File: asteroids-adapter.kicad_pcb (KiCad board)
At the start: 2 copper layers, 88 x 90.2 mm, 15 parts, among them J1 Asteroids PCB connector, J2 Asteroids harness connector, U1 TL074

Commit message: Update to rev 1.3
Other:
- board text added: "Asteroids <-> Ast Deluxe Cabinet Adapter rev 1.3"
- board text removed: "Asteroids <-> Ast Deluxe Cabinet Adapter rev 1.2"
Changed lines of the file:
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@@
   (title_block
     (title "Asteroids to Asteroids Deluxe Adapter")
-    (date "2022-02-22")
-    (rev "1.2")
+    (date "2022-02-24")
+    (rev "1.3")
   )
   (layers
@@
     (effects (font (size 1.905 1.905) (thickness 0.3)) (justify mirror))
   )
-  (gr_text "Asteroids <-> Ast Deluxe Cabinet Adapter rev 1.2" (at 150.5204 62.5856) (layer "F.SilkS")
+  (gr_text "Asteroids <-> Ast Deluxe Cabinet Adapter rev 1.3" (at 150.5204 62.5856) (layer "F.SilkS")
     (effects (font (size 1.524 1.524) (thickness 0.3)))
   )

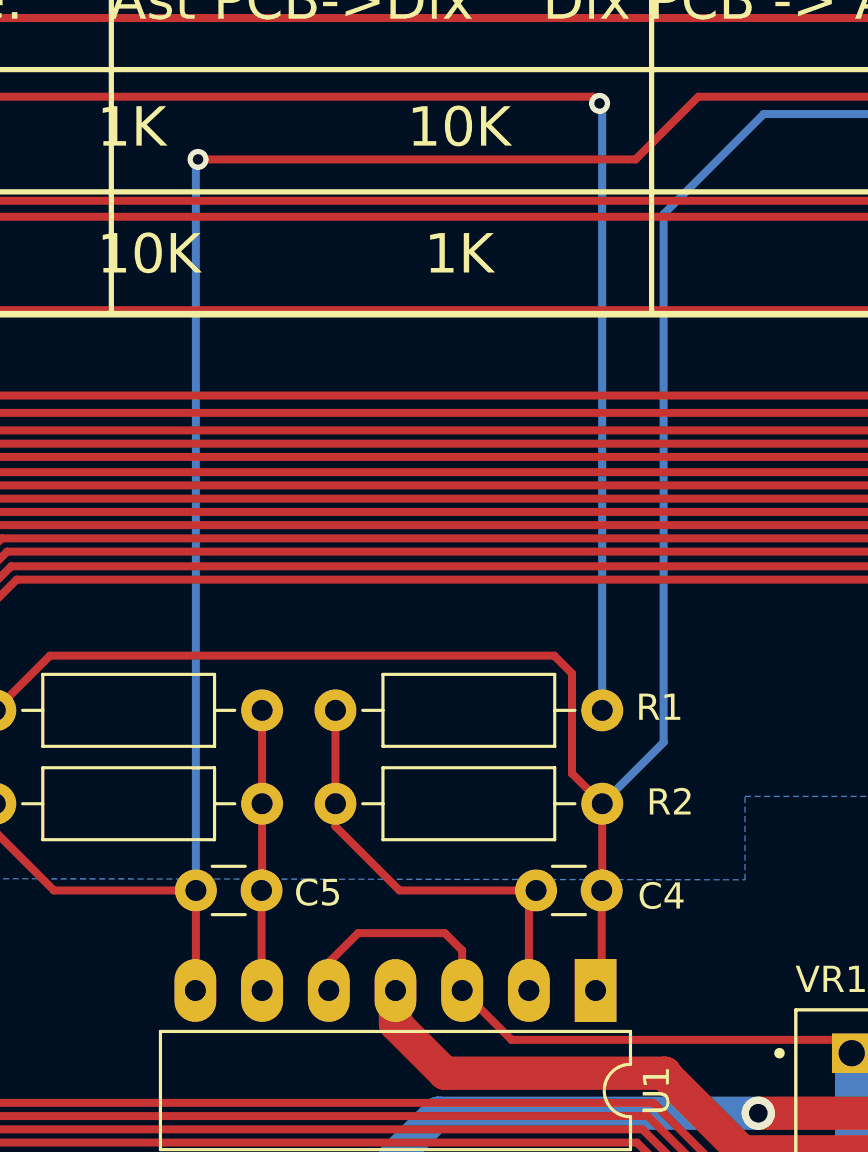
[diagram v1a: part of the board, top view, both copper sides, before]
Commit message: Add bypass to 5V op-amp reference
- Added 10 uf cap at (+) input of both audio inverter op amps, to reduce
noise.
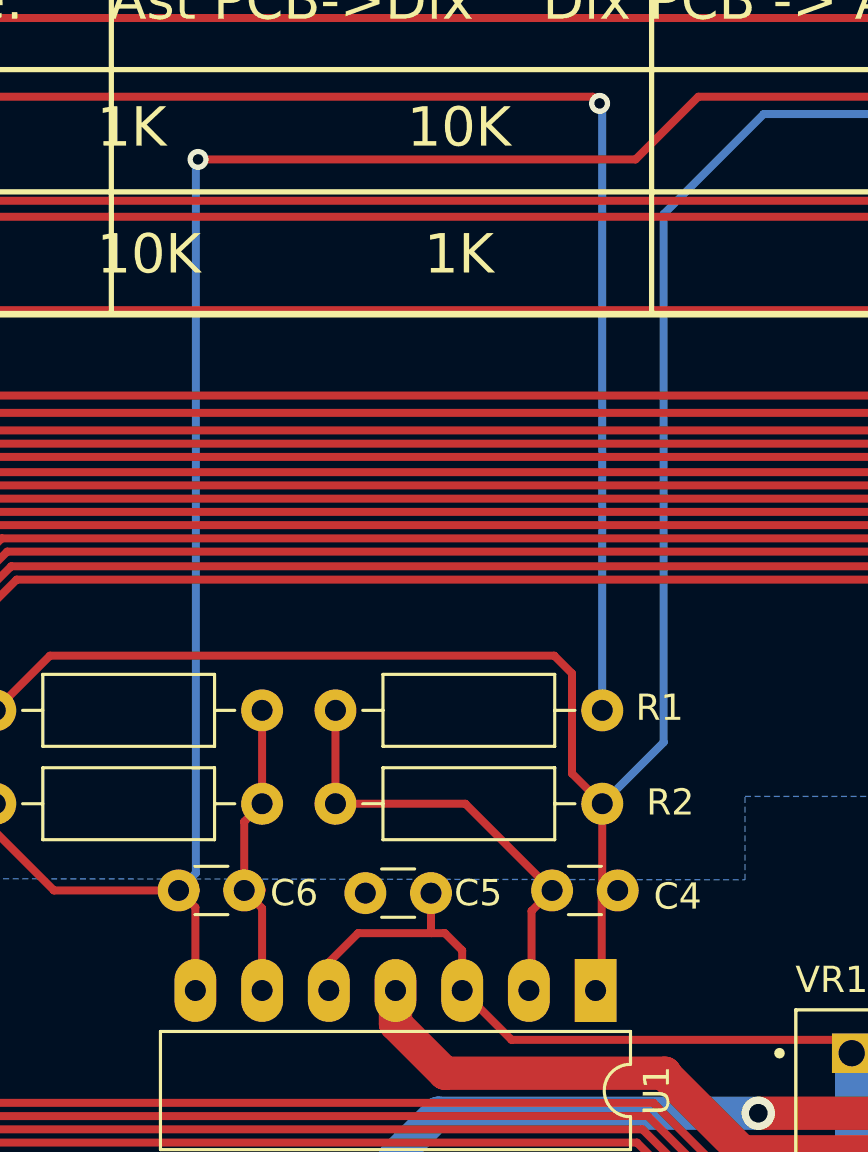
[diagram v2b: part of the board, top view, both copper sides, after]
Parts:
- added C5: Kemet 10 uF 25V MLCC TH, Capacitor_THT:C_Disc_D3.0mm_W1.6mm_P2.50mm, F.Cu at (143.0, 102.1)
- moved C6 0.66 mm to (138.4, 102.0)
- moved C4 0.61 mm to (150.1, 102.0)
- renumbered C5 to C6
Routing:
- net +5V: track 129.9 -> 131.4 mm
- net Net-(C6-Pad1): track 10.7 -> 11.3 mm
- net Audio_2_out: track 96.4 -> 96.9 mm

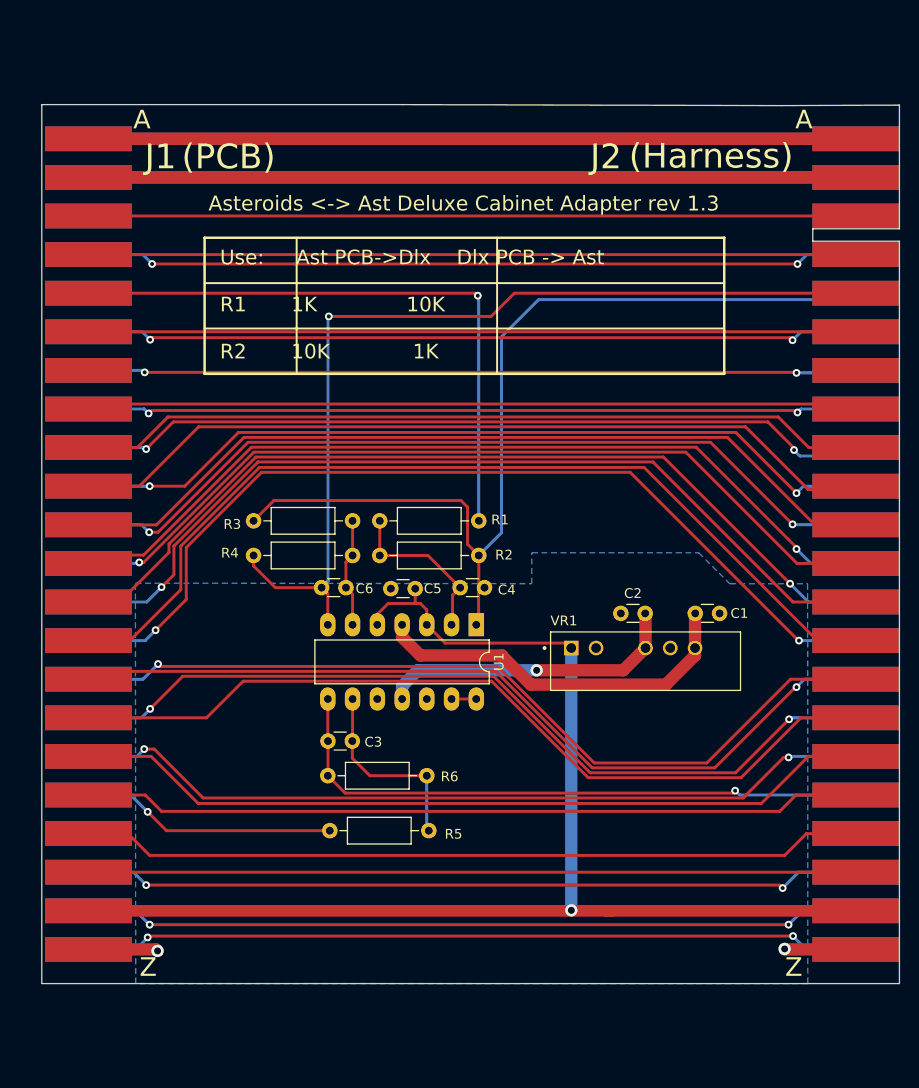
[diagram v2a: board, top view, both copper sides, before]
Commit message: Move parts for narrower design
- Still need to move connector and finish re-routing
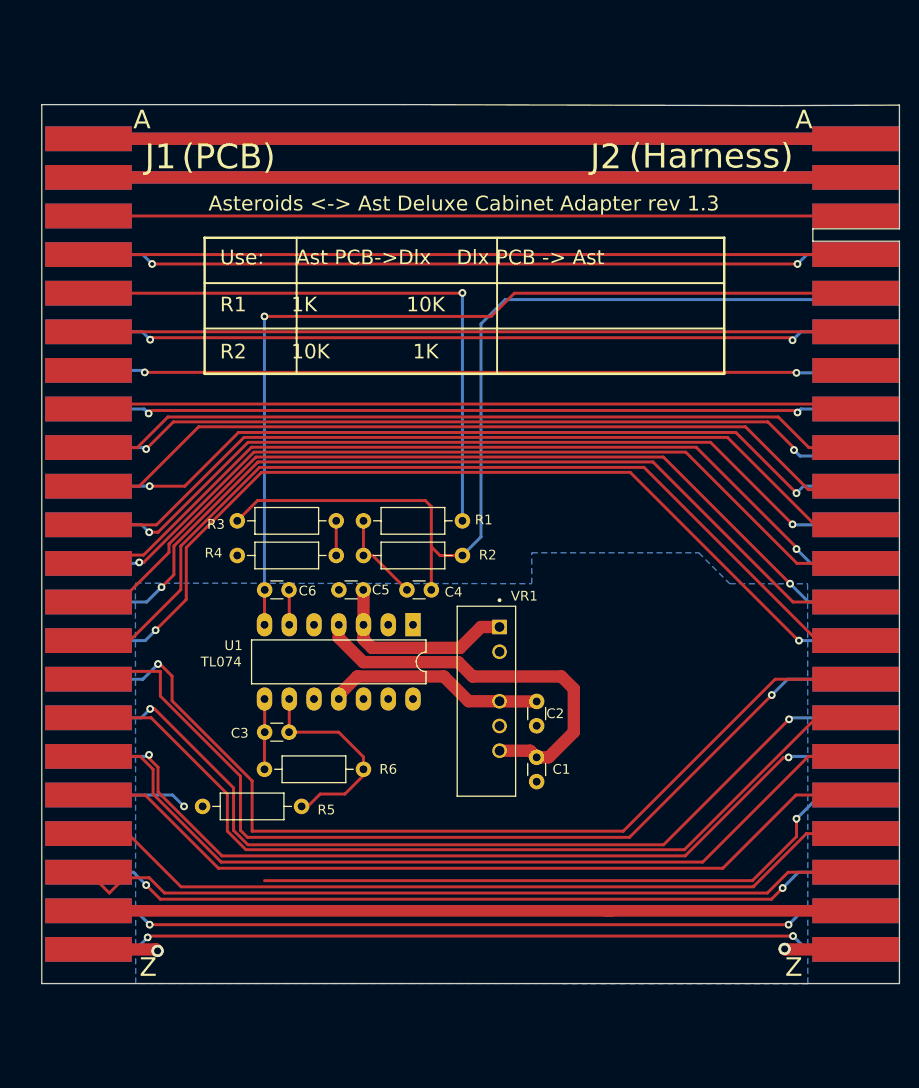
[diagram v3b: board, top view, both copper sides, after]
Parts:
- moved C1 25.5 mm to (158.0, 121.9), turned to 90 degrees
- moved C2 14.4 mm to (158.0, 116.2), turned to 90 degrees
- moved R5 13.3 mm to (133.9, 124.5)
- moved VR1 7.68 mm to (154.2, 106.0), turned to -90 degrees
- moved C3 6.56 mm to (132.6, 116.8)
- moved R6 6.54 mm to (130.0, 120.7)
- moved U1 6.50 mm to (145.3, 105.8)
- moved C6 5.85 mm to (132.6, 102.2)
- moved C4 5.47 mm to (144.7, 102.2)
- moved C5 5.34 mm to (137.7, 102.2)
- moved R1 1.68 mm to (140.2, 95.1)
- moved R2 1.68 mm to (150.4, 98.7)
- moved R3 1.68 mm to (137.4, 95.1)
- moved R4 1.68 mm to (127.3, 98.7)
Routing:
- net +5V: track 131.4 -> 99.1 mm, vias 1 -> 0
- net Y_ORIG: track 30.9 -> 10.3 mm
- net ROT_LEFT: track 86.9 -> 97.6 mm
- net ROT_RIGHT: track 87.2 -> 97.5 mm
- net Y_INV: track 63.1 -> 72.6 mm
- net -15V: track 31.5 -> 22.6 mm, vias 1 -> 0
- net Net-(C4-Pad1): track 17.3 -> 9.48 mm
- net Net-(J1-PadU): track 82.7 -> 89.2 mm
- net Net-(J1-Pad17): track 82.9 -> 89.0 mm
- net Net-(J1-Pad16): track 86.9 -> 92.9 mm
- net Net-(J1-PadT): track 86.9 -> 92.2 mm
- net Net-(J1-PadV): track 80.1 -> 85.0 mm
- net Net-(C6-Pad1): track 11.3 -> 7.15 mm
- net Audio_2_out: track 96.9 -> 93.3 mm
- net Net-(J1-PadX): track 78.7 -> 81.8 mm
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
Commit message: squashed PCB
Still need to clean up PCB outline and re-route
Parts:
- moved J2 19.1 mm to (167.2, 55.9)
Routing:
- net +5V: track 99.1 -> 20.4 mm
- net Net-(J1-PadF): track 78.7 -> 0.00 mm
- net Net-(J1-PadD): track 78.7 -> 0.00 mm
- net Net-(J1-PadC): track 78.7 -> 0.00 mm
- net Net-(J1-PadB): track 78.7 -> 0.00 mm
- net Net-(J1-PadA): track 78.7 -> 0.00 mm
- net Net-(J1-Pad2): track 78.7 -> 0.00 mm
- net Net-(J1-Pad1): track 78.7 -> 0.00 mm
- net Net-(J1-PadJ): track 79.2 -> 1.44 mm
- net Net-(J1-Pad7): track 79.0 -> 12.1 mm
- net Net-(J1-Pad4): track 79.5 -> 13.3 mm
- net Net-(J1-Pad22): track 79.9 -> 13.8 mm
- net Net-(J1-Pad8): track 79.3 -> 13.2 mm
- net Net-(J1-Pad21): track 79.9 -> 14.3 mm
- net Net-(J1-Pad6): track 79.6 -> 14.1 mm
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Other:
- board size 88 x 90.2 mm -> 69 x 90.7 mm
- board text added: "Asteroids <-> Ast Dlx Adapter rev 1.3"
- board text added: "Use: Ast PCB->Dlx Dlx PCB->Ast R1 1K 10K R2 10K 1K"
- board text removed: "Asteroids <-> Ast Deluxe Cabinet Adapter rev 1.3"
- board text removed: "Use: Ast PCB->Dlx Dlx PCB -> Ast R1 1K 10K R2 10K 1K"

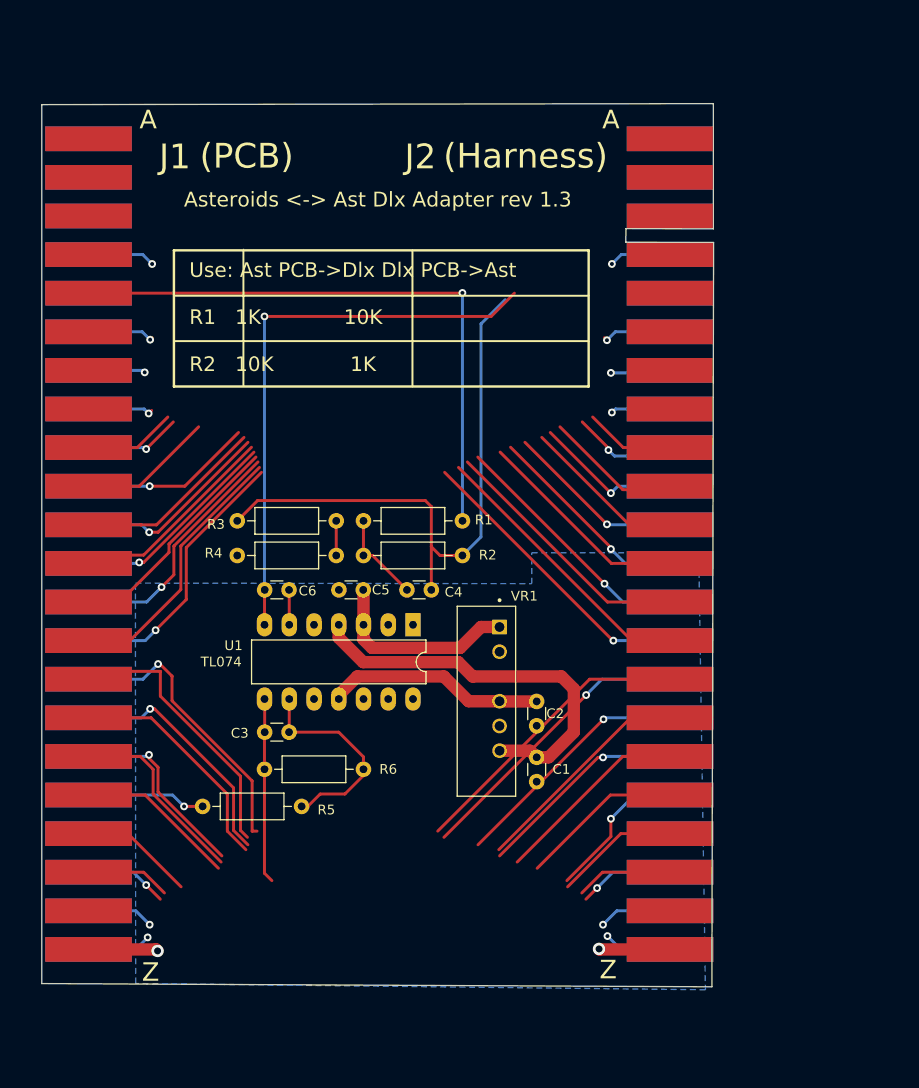
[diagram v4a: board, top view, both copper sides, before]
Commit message: Completed routing on compact PCB
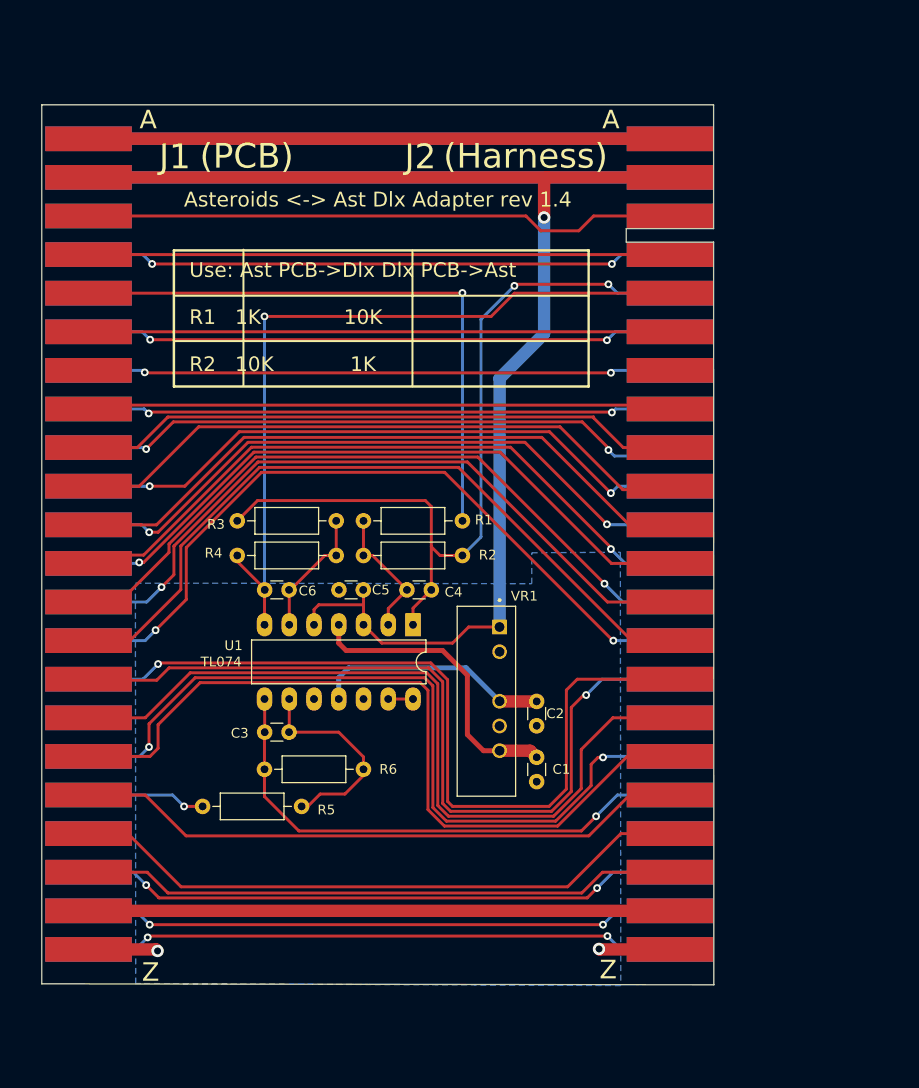
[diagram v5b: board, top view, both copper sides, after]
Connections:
- J1 pad 16: Net-(J1-Pad16) -> unconnected-(J1-Pad16)
- J1 pad B: Net-(J1-PadB) -> +5V
- J1 pad Y: +5V -> Net-(J1-PadY)
- J2 pad 16: Net-(J1-Pad16) -> unconnected-(J2-Pad16)
- J2 pad B: Net-(J1-PadB) -> +5V
- J2 pad Y: +5V -> Net-(J1-PadY)
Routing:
- net +5V: track 20.4 -> 133.7 mm, vias 0 -> 1
- net Net-(J1-PadC): track 0.00 -> 61.0 mm
- net Net-(J1-PadJ): track 1.44 -> 61.5 mm
- net Net-(J1-PadY): track 0.00 -> 59.7 mm
- net Net-(J1-PadF): track 0.00 -> 59.7 mm
- net Net-(J1-PadD): track 0.00 -> 59.7 mm
- net Net-(J1-PadA): track 0.00 -> 59.7 mm
- net Net-(J1-Pad2): track 0.00 -> 59.7 mm
- net Net-(J1-Pad1): track 0.00 -> 59.7 mm
- net Net-(J1-Pad16): track 50.2 -> 0.00 mm, vias 2 -> 0
- net Net-(J1-Pad7): track 12.1 -> 59.9 mm
- net Net-(J1-Pad4): track 13.3 -> 60.5 mm
- net Net-(J1-Pad22): track 13.8 -> 60.8 mm
- net Net-(J1-Pad8): track 13.2 -> 60.1 mm
- net Net-(J1-Pad21): track 14.3 -> 60.9 mm
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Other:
- board size 69 x 90.7 mm -> 69 x 90.3 mm
- board text added: "Asteroids <-> Ast Dlx Adapter rev 1.4"
- board text removed: "Asteroids <-> Ast Dlx Adapter rev 1.3"
